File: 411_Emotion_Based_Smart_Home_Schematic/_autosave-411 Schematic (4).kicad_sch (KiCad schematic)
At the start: 24 parts, among them Q1 NSS1C301ET4G, Q2 NSS1C301ET4G, Q3 NSS1C301ET4G, U4 HC-SR04

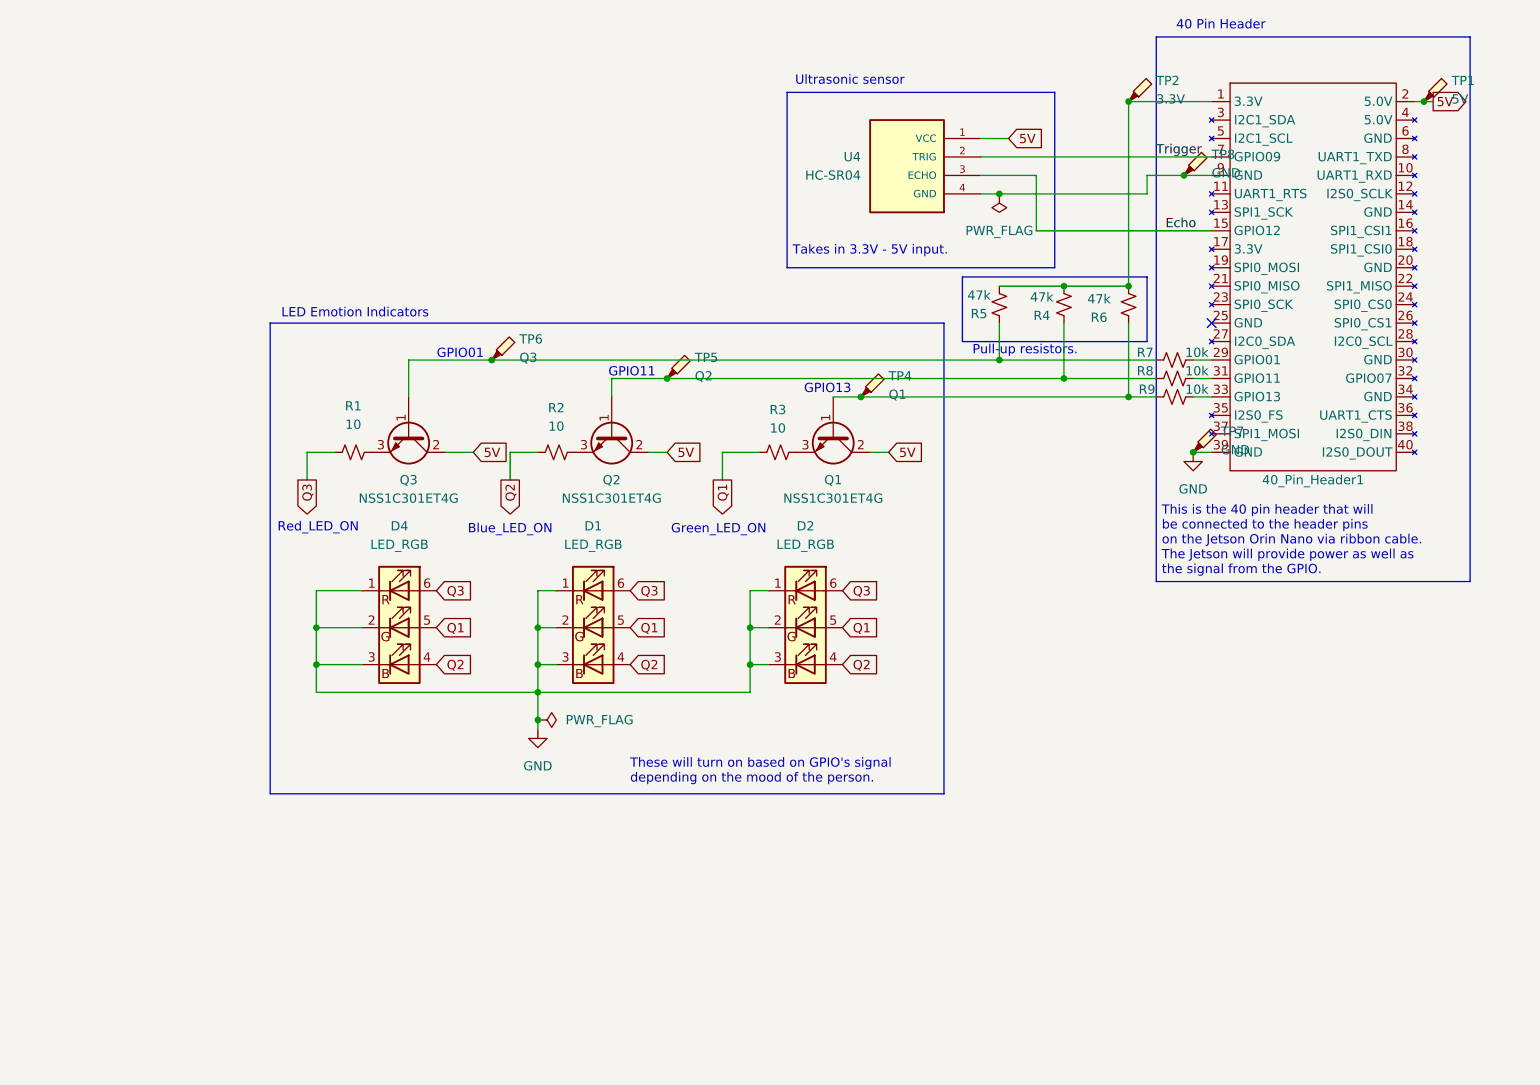
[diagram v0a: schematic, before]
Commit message: Updated schematic.
Added limiting resistors to each GPIO pins.
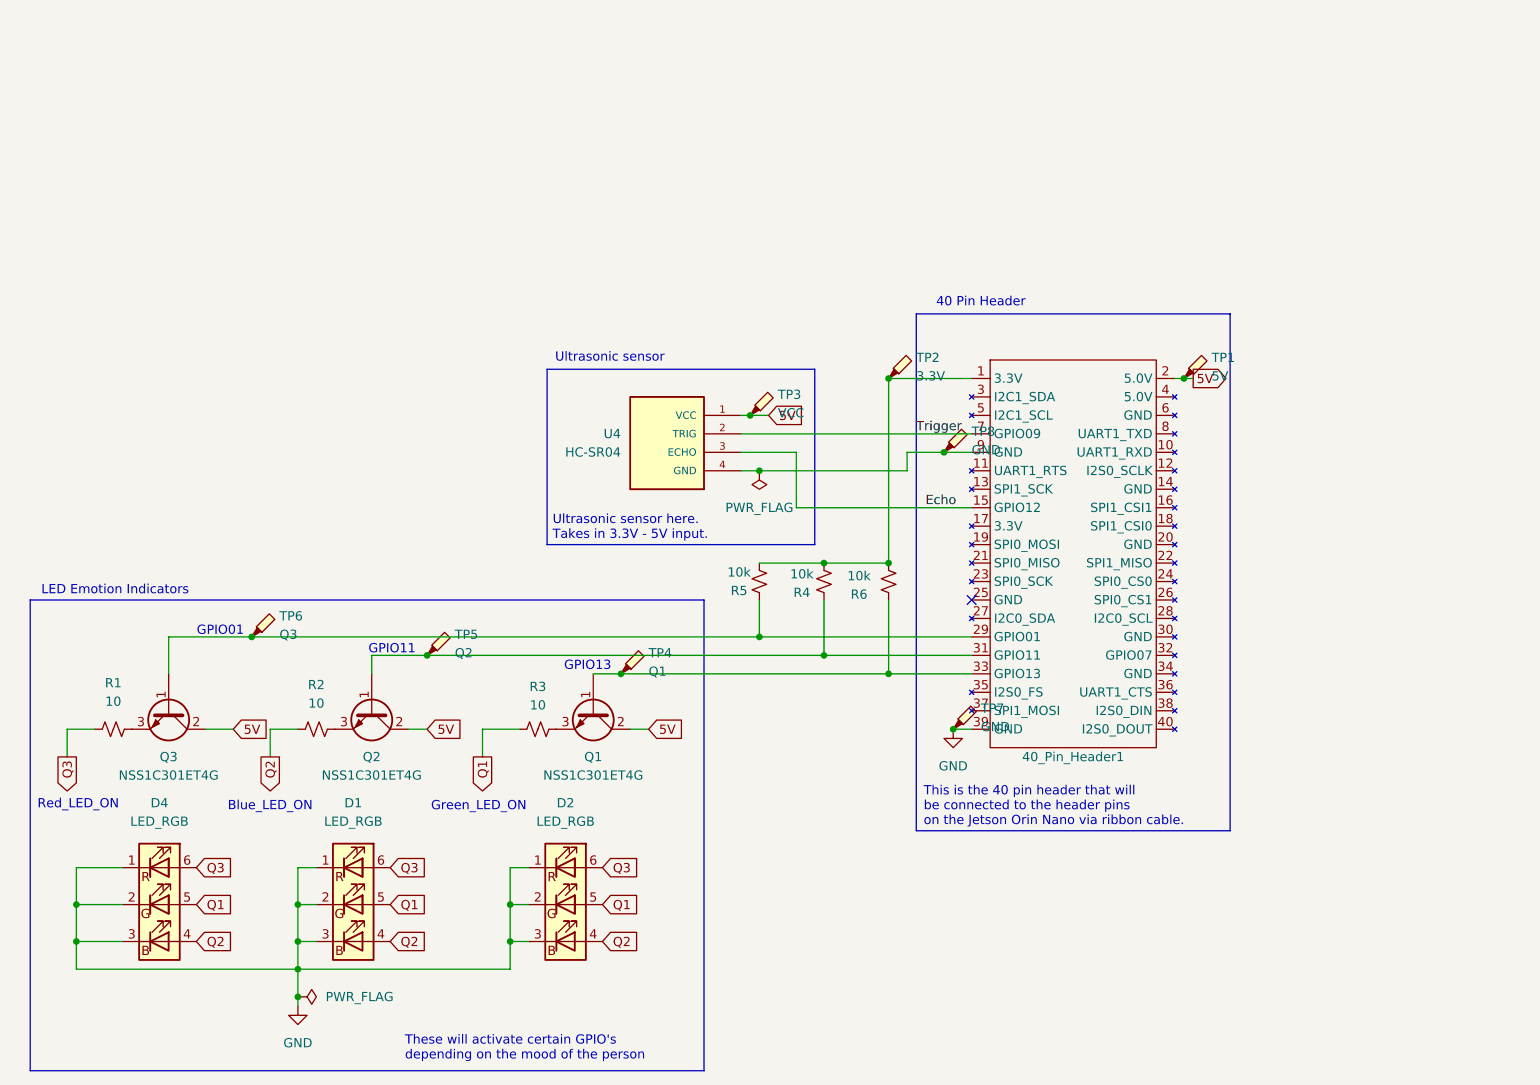
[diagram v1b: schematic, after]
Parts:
- removed R7, R8, R9: 10k, Resistor_THT:R_Axial_DIN0411_L9.9mm_D3.6mm_P5.08mm_Vertical, symbol Device:R_Small_US
- added TP3: VCC, TestPoint:TestPoint_Pad_1.0x1.0mm, symbol Connector:TestPoint_Probe
- R4, R5, R6: value 47k -> 10k
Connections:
- net 5V: now also TP3.1
- net at 40_Pin_Header1.29 (GPIO01): now also Q3.1 (B), R5.2, TP6.1
- net at 40_Pin_Header1.31 (GPIO11): now also Q2.1 (B), R4.2, TP5.1
- net at 40_Pin_Header1.33 (GPIO13): now also Q1.1 (B), R6.2, TP4.1
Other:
- note added: "These will activate certain GPIO's depending on the mood of the person"
- note added: "This is the 40 pin header that will be connected to the header pins on the Jetson Orin Nano via ribbon cable."
- note added: "Ultrasonic sensor here. Takes in 3.3V - 5V input."
- note removed: "Pull-up resistors."
- note removed: "Takes in 3.3V - 5V input."
- note removed: "These will turn on based on GPIO's signal depending on the mood of the person."
- note removed: "This is the 40 pin header that will be connected to the header pins on the Jetson Orin Nano via ribbon cable. The Jetson will provide power as well as the signal from the GPIO."
- moved on the sheet: 40_Pin_Header1, D1, D2, D4, Q1, Q2, Q3, R1, R2, R3, R4, R5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
